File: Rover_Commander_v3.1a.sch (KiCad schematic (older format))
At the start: 73 parts, among them Q1 Crystal KX-7 25MHz, Q2 Crystal KX-7 25MHz, U1 RTL8201CP, U2 L7805ABD2T-TR, U3 H1102NLT, U4 LD1117S33TR_SOT223, U5 STM32F107RCTx, U6 TJA1040T, U7 M95160-WMN6TP

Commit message: fix swd connector, reversed GND and POWER +3.3V
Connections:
- net +3V3_STM: now also XP2.4 (Pin_4); no longer XP2.1 (Pin_1)
- net GND: now also XP2.1 (Pin_1); no longer XP2.4 (Pin_4)
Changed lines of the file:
@@
 L GND #PWR020
 U 1 1 59E0045B
-P 14350 3250
-F 0 "#PWR020" H 14350 3000 50  0001 C CNN
-F 1 "GND" H 14350 3100 50  0000 C CNN
-F 2 "" H 14350 3250 50  0001 C CNN
-F 3 "" H 14350 3250 50  0001 C CNN
-	1    14350 3250
-	-1   0    0    1
+P 14350 3650
+F 0 "#PWR020" H 14350 3400 50  0001 C CNN
+F 1 "GND" H 14350 3500 50  0000 C CNN
+F 2 "" H 14350 3650 50  0001 C CNN
+F 3 "" H 14350 3650 50  0001 C CNN
+	1    14350 3650
+	1    0    0    -1
 $EndComp
 Text Label 13200 2600 0    60   ~ 0
@@
 	-1   0    0    1
 $EndComp
-Text Label 14350 3600 2    60   ~ 0
+Text Label 14350 3300 2    60   ~ 0
 SWD_+3V3
 Text Label 6600 9000 0    60   ~ 0
@@
 	14550 3500 13200 3500
 Wire Wire Line
-	14550 3300 14350 3300
-Wire Wire Line
-	14350 3300 14350 3250
-Wire Wire Line
-	14350 3600 14550 3600
+	14550 3600 14350 3600
+Wire Wire Line
+	14350 3600 14350 3650
+Wire Wire Line
+	14350 3300 14550 3300
 Wire Wire Line
 	13200 2700 14500 2700

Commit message: switch to my library https://github.com/Zulljon/zpkl.git
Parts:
- U2: footprint TO254P1542X460-3N -> zulljon:TO254P1542X460-3N
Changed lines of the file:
@@
 F 0 "U2" H 3000 10400 50  0000 C CNN
 F 1 "L7805ABD2T-TR" H 3000 10000 50  0000 C CNN
-F 2 "TO254P1542X460-3N" H 3000 9900 50  0001 C CNN
+F 2 "zulljon:TO254P1542X460-3N" H 3000 9900 50  0001 C CNN
 F 3 "http://www.st.com/web/en/resource/technical/document/datasheet/CD00000444.pdf" H 3000 9800 50  0001 C CNN
 F 4 "Voltage Regulator 5V 2% 1.5A D2PAK L7805ABD2T-TR, Linear Voltage Regulator, Current Limit, Shut-Down 1.5A 5 V, 2-Pin D2PAK" H 3000 9700 50  0001 C CNN "Description"

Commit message: add transient voltage suppression diods on CAN
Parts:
- added D7, D8: SMAJ33CA-TR, Diodes_SMD:D_SMA, symbol D_TVS
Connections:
- net GND: now also D7.1 (A1), D8.1 (A1)
- net OBD2_CAN_H: now also D7.2 (A2)
- net OBD2_CAN_L: now also D8.2 (A2)
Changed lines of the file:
@@
 ETH_MIO
 $Comp
-L GND #PWR01
+L GND #PWR2
 U 1 1 59DBADE1
 P 1400 7450
-F 0 "#PWR01" H 1400 7200 50  0001 C CNN
+F 0 "#PWR2" H 1400 7200 50  0001 C CNN
 F 1 "GND" H 1400 7300 50  0000 C CNN
 F 2 "" H 1400 7450 50  0001 C CNN
@@
 $EndComp
 $Comp
-L GND #PWR02
+L GND #PWR6
 U 1 1 59DBAE26
 P 3550 7450
-F 0 "#PWR02" H 3550 7200 50  0001 C CNN
+F 0 "#PWR6" H 3550 7200 50  0001 C CNN
 F 1 "GND" H 3550 7300 50  0000 C CNN
 F 2 "" H 3550 7450 50  0001 C CNN
@@
 $EndComp
 $Comp
-L GND #PWR03
+L GND #PWR8
 U 1 1 59DBD7CE
 P 4200 6900
-F 0 "#PWR03" H 4200 6650 50  0001 C CNN
+F 0 "#PWR8" H 4200 6650 50  0001 C CNN
 F 1 "GND" H 4200 6750 50  0000 C CNN
 F 2 "" H 4200 6900 50  0001 C CNN
@@
 $EndComp
 $Comp
-L GND #PWR04
+L GND #PWR11
 U 1 1 59DBD821
 P 4750 6900
-F 0 "#PWR04" H 4750 6650 50  0001 C CNN
+F 0 "#PWR11" H 4750 6650 50  0001 C CNN
 F 1 "GND" H 4750 6750 50  0000 C CNN
 F 2 "" H 4750 6900 50  0001 C CNN
@@
 $EndComp
 $Comp
-L GND #PWR05
+L GND #PWR9
 U 1 1 59DBDF02
 P 4350 4300
-F 0 "#PWR05" H 4350 4050 50  0001 C CNN
+F 0 "#PWR9" H 4350 4050 50  0001 C CNN
 F 1 "GND" H 4350 4150 50  0000 C CNN
 F 2 "" H 4350 4300 50  0001 C CNN
@@
 $EndComp
 $Comp
-L GND #PWR06
+L GND #PWR16
 U 1 1 59DC8831
 P 5550 7700
-F 0 "#PWR06" H 5550 7450 50  0001 C CNN
+F 0 "#PWR16" H 5550 7450 50  0001 C CNN
 F 1 "GND" H 5550 7550 50  0000 C CNN
 F 2 "" H 5550 7700 50  0001 C CNN
@@
 $EndComp
 $Comp
-L GND #PWR07
+L GND #PWR7
 U 1 1 59DC8898
 P 4050 7700
-F 0 "#PWR07" H 4050 7450 50  0001 C CNN
+F 0 "#PWR7" H 4050 7450 50  0001 C CNN
 F 1 "GND" H 4050 7550 50  0000 C CNN
 F 2 "" H 4050 7700 50  0001 C CNN
@@
 $EndComp
 $Comp
-L GND #PWR08
+L GND #PWR10
 U 1 1 59DC88E8
 P 4650 7700
-F 0 "#PWR08" H 4650 7450 50  0001 C CNN
+F 0 "#PWR10" H 4650 7450 50  0001 C CNN
 F 1 "GND" H 4650 7550 50  0000 C CNN
 F 2 "" H 4650 7700 50  0001 C CNN
@@
 $EndComp
 $Comp
-L GND #PWR09
+L GND #PWR14
 U 1 1 59DC9346
 P 5250 7700
-F 0 "#PWR09" H 5250 7450 50  0001 C CNN
+F 0 "#PWR14" H 5250 7450 50  0001 C CNN
 F 1 "GND" H 5250 7550 50  0000 C CNN
 F 2 "" H 5250 7700 50  0001 C CNN
@@
 $EndComp
 $Comp
-L GND #PWR010
+L GND #PWR12
 U 1 1 59DC939C
 P 4950 7700
-F 0 "#PWR010" H 4950 7450 50  0001 C CNN
+F 0 "#PWR12" H 4950 7450 50  0001 C CNN
 F 1 "GND" H 4950 7550 50  0000 C CNN
 F 2 "" H 4950 7700 50  0001 C CNN
@@
 $EndComp
 $Comp
-L GND #PWR011
+L GND #PWR15
 U 1 1 59DDCEC6
 P 5500 2750
-F 0 "#PWR011" H 5500 2500 50  0001 C CNN
+F 0 "#PWR15" H 5500 2500 50  0001 C CNN
 F 1 "GND" H 5500 2600 50  0000 C CNN
 F 2 "" H 5500 2750 50  0001 C CNN
@@
 $EndComp
 $Comp
-L GND #PWR012
+L GND #PWR5
 U 1 1 59DDEFAF
 P 2200 3850
-F 0 "#PWR012" H 2200 3600 50  0001 C CNN
+F 0 "#PWR5" H 2200 3600 50  0001 C CNN
 F 1 "GND" H 2200 3700 50  0000 C CNN
 F 2 "" H 2200 3850 50  0001 C CNN
@@
 $EndComp
 $Comp
-L GND #PWR013
+L GND #PWR3
 U 1 1 59DDF0B0
 P 1700 3850
-F 0 "#PWR013" H 1700 3600 50  0001 C CNN
+F 0 "#PWR3" H 1700 3600 50  0001 C CNN
 F 1 "GND" H 1700 3700 50  0000 C CNN
 F 2 "" H 1700 3850 50  0001 C CNN
@@
 $EndComp
 $Comp
-L GND #PWR014
+L GND #PWR1
 U 1 1 59DDF136
 P 1200 3850
-F 0 "#PWR014" H 1200 3600 50  0001 C CNN
+F 0 "#PWR1" H 1200 3600 50  0001 C CNN
 F 1 "GND" H 1200 3700 50  0000 C CNN
 F 2 "" H 1200 3850 50  0001 C CNN
@@
 USB_D-
 $Comp
-L GND #PWR015
+L GND #PWR22
 U 1 1 59DE2DFD
 P 9800 9200
-F 0 "#PWR015" H 9800 8950 50  0001 C CNN
+F 0 "#PWR22" H 9800 8950 50  0001 C CNN
 F 1 "GND" H 9800 9050 50  0000 C CNN
 F 2 "" H 9800 9200 50  0001 C CNN
@@
 $EndComp
 $Comp
-L GND #PWR016
+L GND #PWR19
 U 1 1 59DE81C6
 P 6650 2700
-F 0 "#PWR016" H 6650 2450 50  0001 C CNN
+F 0 "#PWR19" H 6650 2450 50  0001 C CNN
 F 1 "GND" H 6650 2550 50  0000 C CNN
 F 2 "" H 6650 2700 50  0001 C CNN
@@
 $EndComp
 $Comp
-L GND #PWR017
+L GND #PWR20
 U 1 1 59DE81CC
 P 6650 3250
-F 0 "#PWR017" H 6650 3000 50  0001 C CNN
+F 0 "#PWR20" H 6650 3000 50  0001 C CNN
 F 1 "GND" H 6650 3100 50  0000 C CNN
 F 2 "" H 6650 3250 50  0001 C CNN
@@
 $EndComp
 $Comp
-L GND #PWR018
+L GND #PWR23
 U 1 1 59DE9354
 P 10300 5800
-F 0 "#PWR018" H 10300 5550 50  0001 C CNN
+F 0 "#PWR23" H 10300 5550 50  0001 C CNN
 F 1 "GND" H 10300 5650 50  0000 C CNN
 F 2 "" H 10300 5800 50  0001 C CNN
@@
 $EndComp
 $Comp
-L GND #PWR019
+L GND #PWR30
 U 1 1 59DFDDAC
 P 14650 2250
-F 0 "#PWR019" H 14650 2000 50  0001 C CNN
+F 0 "#PWR30" H 14650 2000 50  0001 C CNN
 F 1 "GND" H 14650 2100 50  0000 C CNN
 F 2 "" H 14650 2250 50  0001 C CNN
@@
 $EndComp
 $Comp
-L GND #PWR020
+L GND #PWR29
 U 1 1 59E0045B
 P 14350 3650
-F 0 "#PWR020" H 14350 3400 50  0001 C CNN
+F 0 "#PWR29" H 14350 3400 50  0001 C CNN
 F 1 "GND" H 14350 3500 50  0000 C CNN
 F 2 "" H 14350 3650 50  0001 C CNN
@@
 BUZZER
 $Comp
-L GND #PWR021
+L GND #PWR31
 U 1 1 59E058A9
 P 15150 2000
-F 0 "#PWR021" H 15150 1750 50  0001 C CNN
+F 0 "#PWR31" H 15150 1750 50  0001 C CNN
 F 1 "GND" H 15150 1850 50  0000 C CNN
 F 2 "" H 15150 2000 50  0001 C CNN
@@
 $EndComp
 $Comp
-L GND #PWR022
+L GND #PWR28
 U 1 1 59E08000
 P 14200 6900
-F 0 "#PWR022" H 14200 6650 50  0001 C CNN
+F 0 "#PWR28" H 14200 6650 50  0001 C CNN
 F 1 "GND" H 14200 6750 50  0000 C CNN
 F 2 "" H 14200 6900 50  0001 C CNN
@@
 $EndComp
 $Comp
-L GND #PWR023
+L GND #PWR27
 U 1 1 59E08A4A
 P 13650 7050
-F 0 "#PWR023" H 13650 6800 50  0001 C CNN
+F 0 "#PWR27" H 13650 6800 50  0001 C CNN
 F 1 "GND" H 13650 6900 50  0000 C CNN
 F 2 "" H 13650 7050 50  0001 C CNN
@@
 $EndComp
 $Comp
-L GND #PWR024
+L GND #PWR34
 U 1 1 59E091E1
 P 15700 6950
-F 0 "#PWR024" H 15700 6700 50  0001 C CNN
+F 0 "#PWR34" H 15700 6700 50  0001 C CNN
 F 1 "GND" H 15700 6800 50  0000 C CNN
 F 2 "" H 15700 6950 50  0001 C CNN
@@
 $EndComp
 $Comp
-L GND #PWR025
+L GND #PWR4
 U 1 1 59E20129
 P 1900 10700
-F 0 "#PWR025" H 1900 10450 50  0001 C CNN
+F 0 "#PWR4" H 1900 10450 50  0001 C CNN
 F 1 "GND" H 1900 10550 50  0000 C CNN
 F 2 "" H 1900 10700 50  0001 C CNN
@@
 $EndComp
 $Comp
-L GND #PWR026
+L GND #PWR21
 U 1 1 59E233AC
 P 8850 6250
-F 0 "#PWR026" H 8850 6000 50  0001 C CNN
+F 0 "#PWR21" H 8850 6000 50  0001 C CNN
 F 1 "GND" H 8850 6100 50  0000 C CNN
 F 2 "" H 8850 6250 50  0001 C CNN
@@
 ETH_RST
 $Comp
-L GND #PWR027
+L GND #PWR25
 U 1 1 59E3E2A9
 P 11500 8800
-F 0 "#PWR027" H 11500 8550 50  0001 C CNN
+F 0 "#PWR25" H 11500 8550 50  0001 C CNN
 F 1 "GND" H 11500 8650 50  0000 C CNN
 F 2 "" H 11500 8800 50  0001 C CNN
@@
 $EndComp
 $Comp
-L GND #PWR028
+L GND #PWR17
 U 1 1 59E06DCA
 P 5650 6900
-F 0 "#PWR028" H 5650 6650 50  0001 C CNN
+F 0 "#PWR17" H 5650 6650 50  0001 C CNN
 F 1 "GND" H 5650 6750 50  0000 C CNN
 F 2 "" H 5650 6900 50  0001 C CNN
@@
 $EndComp
 $Comp
-L GND #PWR029
+L GND #PWR18
 U 1 1 59E06DD0
 P 6350 6900
-F 0 "#PWR029" H 6350 6650 50  0001 C CNN
+F 0 "#PWR18" H 6350 6650 50  0001 C CNN
 F 1 "GND" H 6350 6750 50  0000 C CNN
 F 2 "" H 6350 6900 50  0001 C CNN
@@
 $EndComp
 $Comp
-L GND #PWR030
+L GND #PWR13
 U 1 1 59E06DDC
 P 5200 6900
-F 0 "#PWR030" H 5200 6650 50  0001 C CNN
+F 0 "#PWR13" H 5200 6650 50  0001 C CNN
 F 1 "GND" H 5200 6750 50  0000 C CNN
 F 2 "" H 5200 6900 50  0001 C CNN
@@
 EEPROM_CS
 $Comp
-L GND #PWR031
+L GND #PWR24
 U 1 1 59E54E88
 P 10350 7450
-F 0 "#PWR031" H 10350 7200 50  0001 C CNN
+F 0 "#PWR24" H 10350 7200 50  0001 C CNN
 F 1 "GND" H 10350 7300 50  0000 C CNN
 F 2 "" H 10350 7450 50  0001 C CNN
@@
 $EndComp
 $Comp
-L GND #PWR032
+L GND #PWR26
 U 1 1 59E565CA
 P 12500 7350
-F 0 "#PWR032" H 12500 7100 50  0001 C CNN
+F 0 "#PWR26" H 12500 7100 50  0001 C CNN
 F 1 "GND" H 12500 7200 50  0000 C CNN
 F 2 "" H 12500 7350 50  0001 C CNN
@@
 $EndComp
 $Comp
-L PWR_FLAG #FLG033
+L PWR_FLAG #FLG1
 U 1 1 59E7776C
 P 1300 10200
-F 0 "#FLG033" H 1300 10275 50  0001 C CNN
+F 0 "#FLG1" H 1300 10275 50  0001 C CNN
 F 1 "PWR_FLAG" H 1200 10350 50  0000 C CNN
 F 2 "" H 1300 10200 50  0001 C CNN
@@
 Connection ~ 5900 9750
 $Comp
-L PWR_FLAG #FLG034
+L PWR_FLAG #FLG4
 U 1 1 59E8194E
 P 6500 9000
-F 0 "#FLG034" H 6500 9075 50  0001 C CNN
+F 0 "#FLG4" H 6500 9075 50  0001 C CNN
 F 1 "PWR_FLAG" H 6500 9150 50  0000 C CNN
 F 2 "" H 6500 9000 50  0001 C CNN
@@
 Connection ~ 3550 6750
 $Comp
-L PWR_FLAG #FLG035
+L PWR_FLAG #FLG3
 U 1 1 59E86DF2
 P 5850 9750
-F 0 "#FLG035" H 5850 9825 50  0001 C CNN
+F 0 "#FLG3" H 5850 9825 50  0001 C CNN
 F 1 "PWR_FLAG" H 5850 9900 50  0000 C CNN
 F 2 "" H 5850 9750 50  0001 C CNN
@@
 $EndComp
 $Comp
-L PWR_FLAG #FLG036
+L PWR_FLAG #FLG2
 U 1 1 59E872CF
 P 4600 9800
-F 0 "#FLG036" H 4600 9875 50  0001 C CNN
+F 0 "#FLG2" H 4600 9875 50  0001 C CNN
 F 1 "PWR_FLAG" H 4600 9950 50  0000 C CNN
 F 2 "" H 4600 9800 50  0001 C CNN
@@
 	3700 10250 3700 10650
 Connection ~ 3700 10650
+$Comp
+L D_TVS D7
+U 1 1 5A18125C
+P 15300 6100
+F 0 "D7" V 15300 6200 50  0000 C CNN
+F 1 "SMAJ33CA-TR" V 15350 6400 50  0000 C CNN
+F 2 "Diodes_SMD:D_SMA" H 15300 6100 50  0001 C CNN
+F 3 "" H 15300 6100 50  0001 C CNN
+	1    15300 6100
+	0    1    1    0
+$EndComp
+$Comp
+L D_TVS D8
+U 1 1 5A182F4A
+P 15300 6800
+F 0 "D8" V 15300 6900 50  0000 C CNN
+F 1 "SMAJ33CA-TR" V 15350 7100 50  0000 C CNN
+F 2 "Diodes_SMD:D_SMA" H 15300 6800 50  0001 C CNN
+F 3 "" H 15300 6800 50  0001 C CNN
+	1    15300 6800
+	0    -1   -1   0
+$EndComp
+$Comp
+L GND #PWR33
+U 1 1 5A183272
+P 15300 7000
+F 0 "#PWR33" H 15300 6750 50  0001 C CNN
+F 1 "GND" H 15300 6850 50  0000 C CNN
+F 2 "" H 15300 7000 50  0001 C CNN
+F 3 "" H 15300 7000 50  0001 C CNN
+	1    15300 7000
+	1    0    0    -1
+$EndComp
+Wire Wire Line
+	15300 7000 15300 6950
+Wire Wire Line
+	15300 6650 15300 6550
+Connection ~ 15300 6550
+Wire Wire Line
+	15300 6350 15300 6250
+Connection ~ 15300 6350
+Wire Wire Line
+	15300 5950 15300 5900
+$Comp
+L GND #PWR32
+U 1 1 5A183922
+P 15300 5900
+F 0 "#PWR32" H 15300 5650 50  0001 C CNN
+F 1 "GND" H 15300 5750 50  0000 C CNN
+F 2 "" H 15300 5900 50  0001 C CNN
+F 3 "" H 15300 5900 50  0001 C CNN
+	1    15300 5900
+	-1   0    0    1
+$EndComp
 $EndSCHEMATC

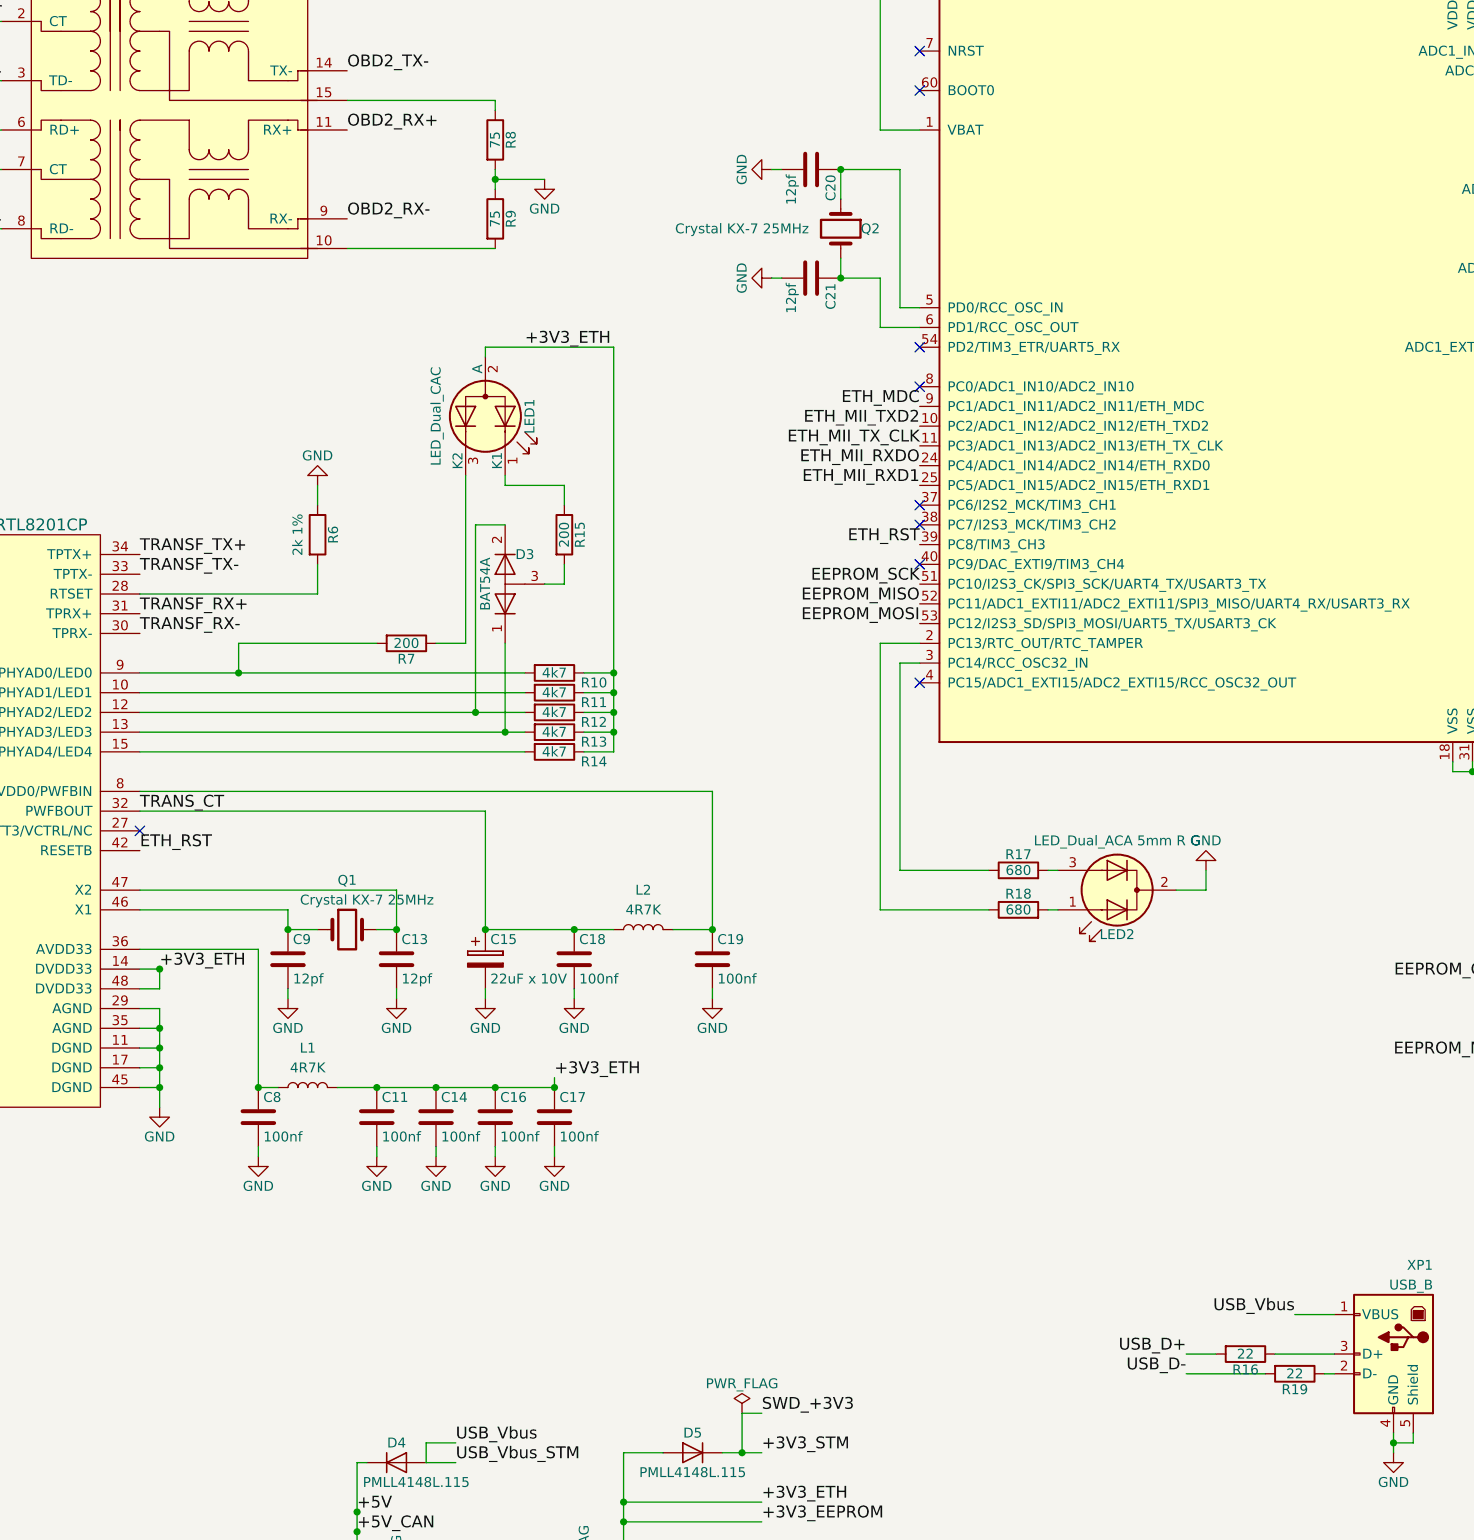
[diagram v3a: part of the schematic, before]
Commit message: fix crystals package, add thermo-pads to voltage regulator, fix usb like differential pair
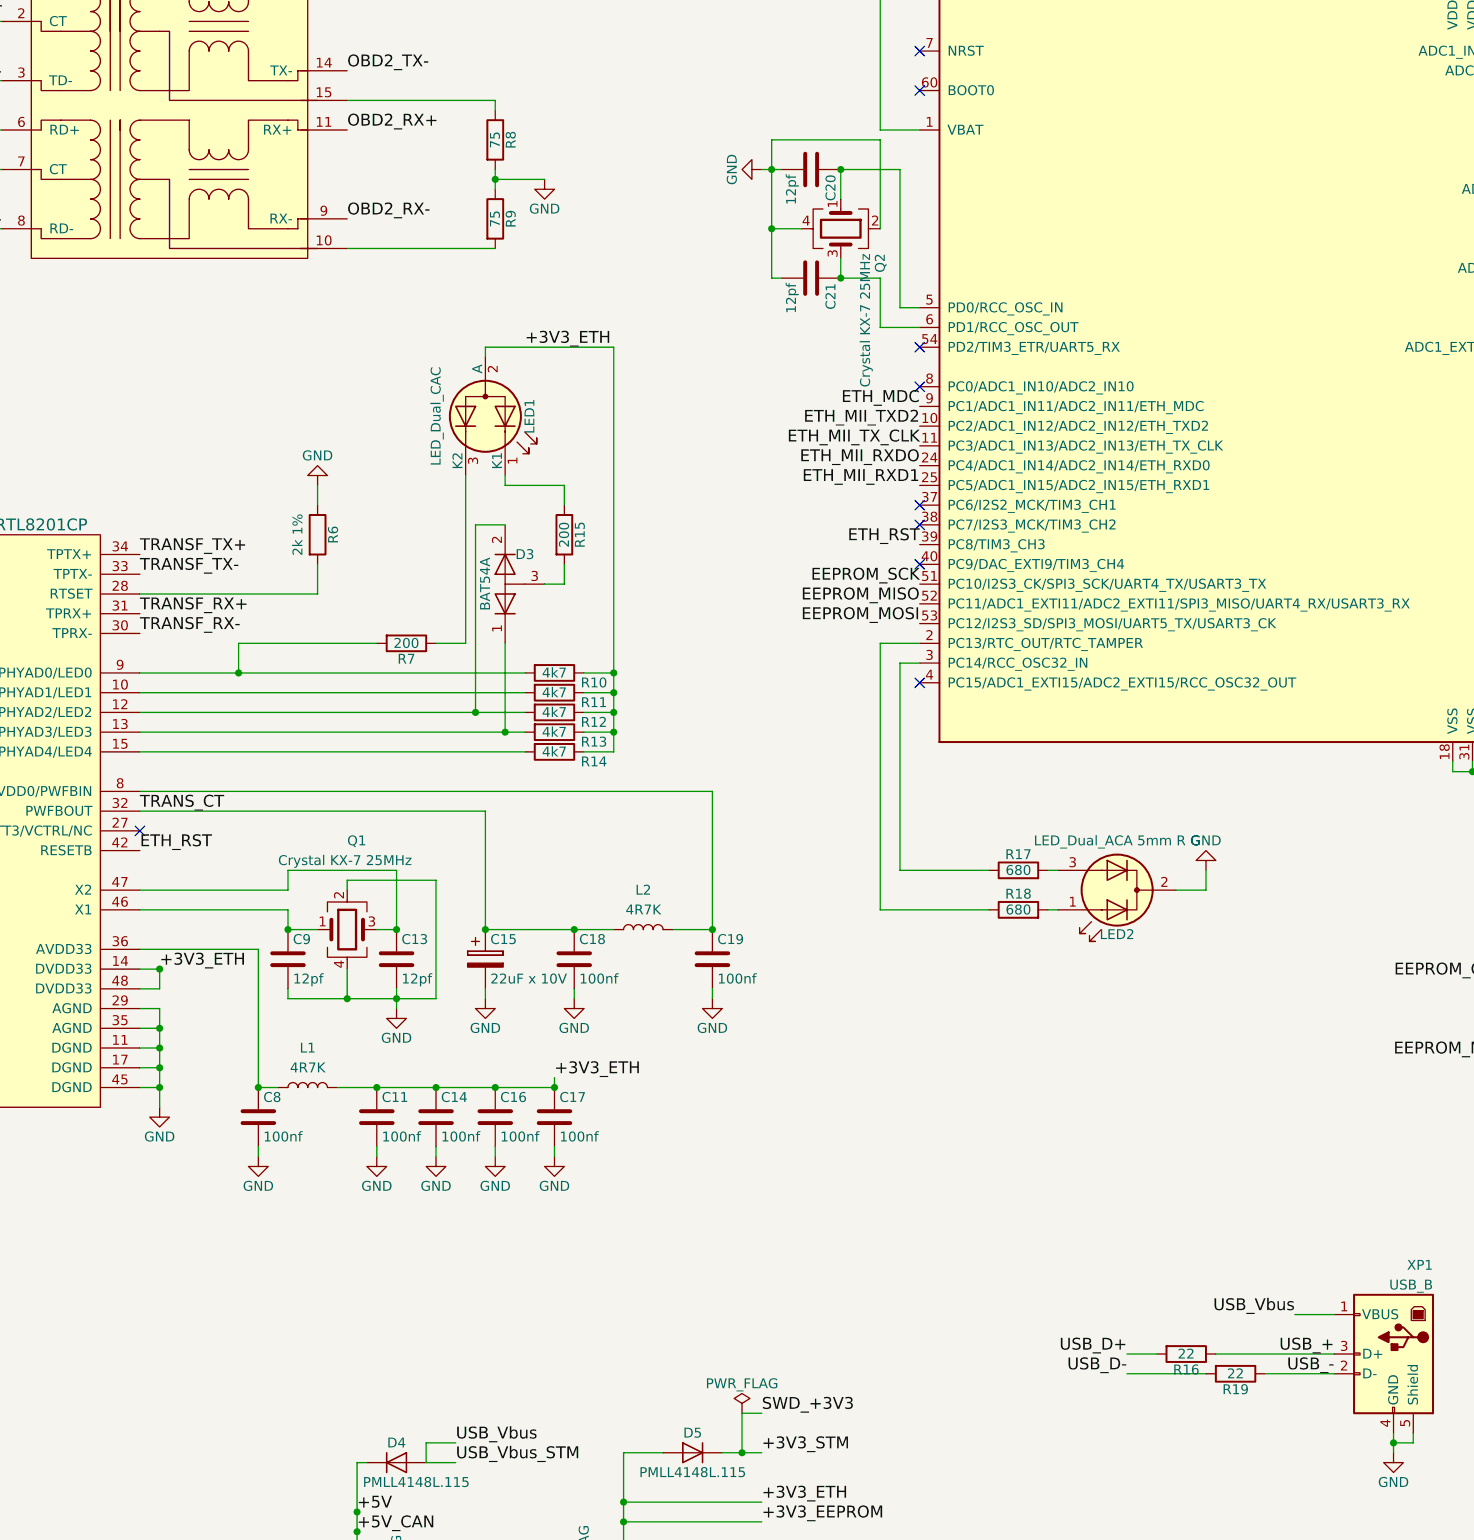
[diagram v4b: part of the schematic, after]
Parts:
- removed Q1, Q2: Crystal KX-7 25MHz, Crystals:Crystal_SMD_7050-4pin_7.0x5.0mm, symbol Crystal
- added Q1, Q2: Crystal KX-7 25MHz, Crystals:Crystal_SMD_7050-4pin_7.0x5.0mm, symbol Crystal_GND24
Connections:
- net GND: now also Q1.2, Q1.4, Q2.2, Q2.4
- net at C20.1, U5.5 (PD0/RCC_OSC_IN): now also Q2.1
- net at C21.1, U5.6 (PD1/RCC_OSC_OUT): now also Q2.3
- net USB_-: now reaches R19.1, XP1.2 (D-)
- net USB_+: now reaches R16.1, XP1.3 (D+)
- net at C9.1, U1.46 (X1): now also Q1.1
- net at C13.1, U1.47 (X2): now also Q1.3
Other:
- moved on the sheet: R16, R19
